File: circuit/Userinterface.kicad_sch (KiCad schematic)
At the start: 33 parts, among them J9 Micro_SD_Card_Det_Hirose_DM3AT, Q10 DMN1054UCB4, Q9 DMP1100UCB4-7, SW3 FR01FR16P-S, SW4 SKRHAAE010, U8 SSD1351

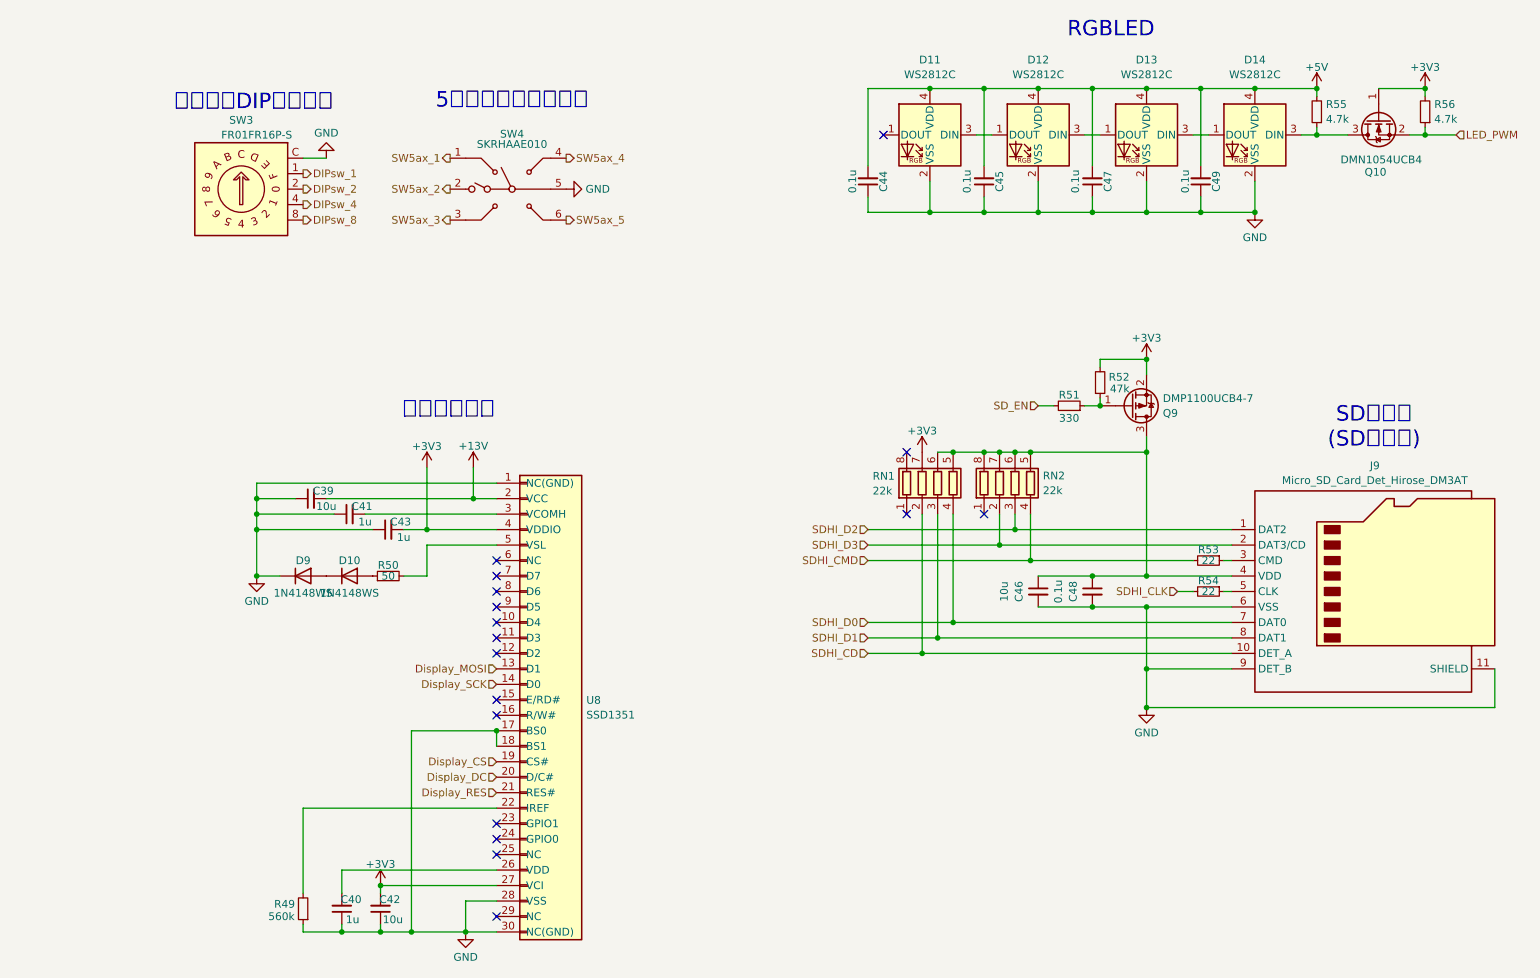
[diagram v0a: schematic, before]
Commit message: スマコンの設定変更 回路図変更
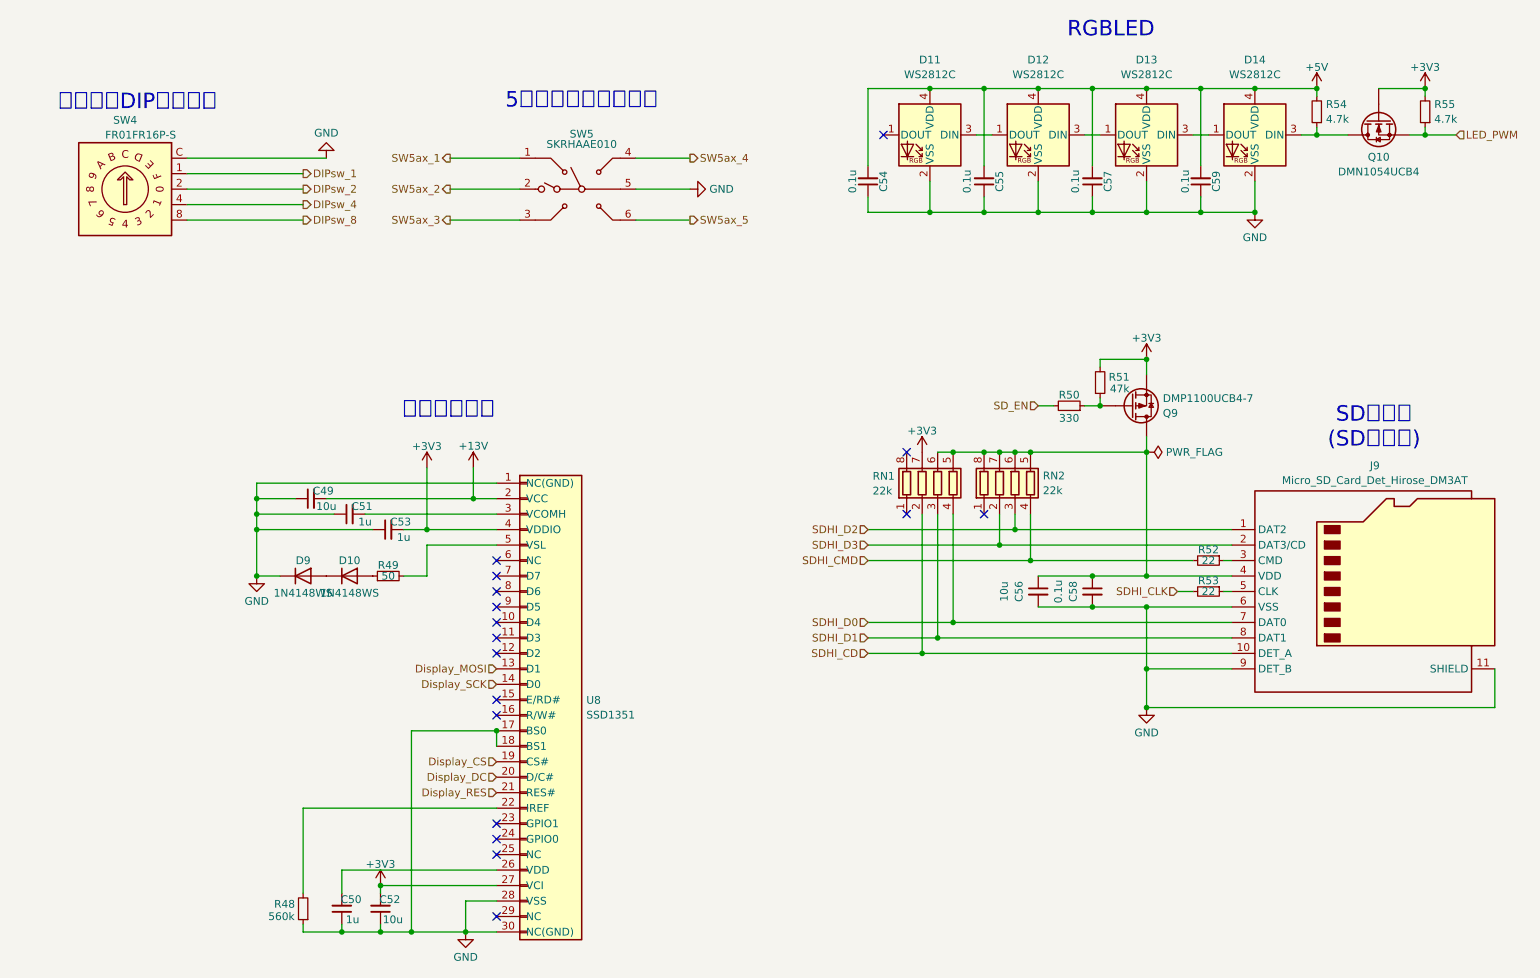
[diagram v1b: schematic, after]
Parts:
- removed Q10: DMN1054UCB4, robot_contest:DMN1054UCB4, symbol Device:Q_NMOS_GSD
- removed Q9: DMP1100UCB4-7, robot_contest:DMN1054UCB4, symbol Device:Q_PMOS_GSD
- added Q10: DMN1054UCB4, robot_contest:DMN1054UCB4, symbol Device:Q_NMOS
- added Q9: DMP1100UCB4-7, robot_contest:DMN1054UCB4, symbol Device:Q_PMOS
- D11, D12, D13, D14: symbol robocon:WS2812C -> robot_contest:WS2812C
- SW5: renamed from SW4; footprint robot_contest:SKRHAAE010 -> robot_contest:SKRHABE010; symbol robocon:SKRHABE010 -> robot_contest:SKRHABE010
- U8: symbol robocon:SSD1351 -> robot_contest:SSD1351
- renumbered C39 to C49, C40 to C50, C41 to C51, C42 to C52, C43 to C53, C44 to C54, C45 to C55, C46 to C56, C47 to C57, C48 to C58, C49 to C59, R49 to R48, R50 to R49, R51 to R50, R52 to R51, R53 to R52, R54 to R53, R55 to R54, R56 to R55, SW3 to SW4
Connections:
- net +3V3: now also Q10.G, Q9.S
- net LED_PWM: now also Q10.S
- net at C56.1, C58.1, J9.4 (VDD)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: now also Q9.D
- net at D14.3 (DIN), R54.1: now also Q10.D
- net at R50.1, R51.1: now also Q9.G
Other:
- moved on the sheet: SW4, SW5
